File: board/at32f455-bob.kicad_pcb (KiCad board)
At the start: 2 copper layers, 66 parts, among them J1 BB, J2 PWR, J3 PROG, J4 CAN, J5 RS486, J6 USB_C_Receptacle, J7 +3.3V, J8 +5V, SW1 RotaryEncoder_Switch, SW2 RESET, SW3 BTL, U1 LM1117MP-3.3, U2 AT32F455CxT7, U3 PAN2110P0AA, U4 HMT1040T, U5 ST3485EB, U6 ER_OLEDM0.91_1x-I2C, Y1 not populated, Y2 16MHz

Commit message: WIP
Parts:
- J4, J5: footprint Connector_Phoenix_MC:PhoenixContact_MCV_1,5_3-G-3.5_1x03_P3.50mm_Vertical -> Connector_Phoenix_MC:PhoenixContact_MC_1,5_3-G-3.5_1x03_P3.50mm_Horizontal
- J7, J8: footprint Connector_Phoenix_MC:PhoenixContact_MCV_1,5_2-G-3.5_1x02_P3.50mm_Vertical -> Connector_Phoenix_MC:PhoenixContact_MC_1,5_2-G-3.5_1x02_P3.50mm_Horizontal
- moved D4 146.9 mm to (209.4, 52.0)
- moved D5 146.9 mm to (209.4, 55.1)
- moved SW1 146.9 mm to (204.8, 28.4)
- moved C16 146.9 mm to (209.4, 40.0)
- moved C17 146.9 mm to (209.4, 43.0)
- moved C18 146.9 mm to (209.4, 46.0)
- moved C19 146.9 mm to (209.4, 49.0)
- moved D6 146.9 mm to (215.7, 41.8)
- moved R10 146.9 mm to (205.0, 51.8)
- moved R11 146.9 mm to (205.0, 54.7)
- moved R12 146.9 mm to (205.0, 57.6)
- moved R13 146.9 mm to (205.0, 60.6)
- moved R6 146.9 mm to (205.0, 40.0)
- moved R7 146.9 mm to (205.0, 42.9)
- moved R8 146.9 mm to (205.0, 45.9)
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
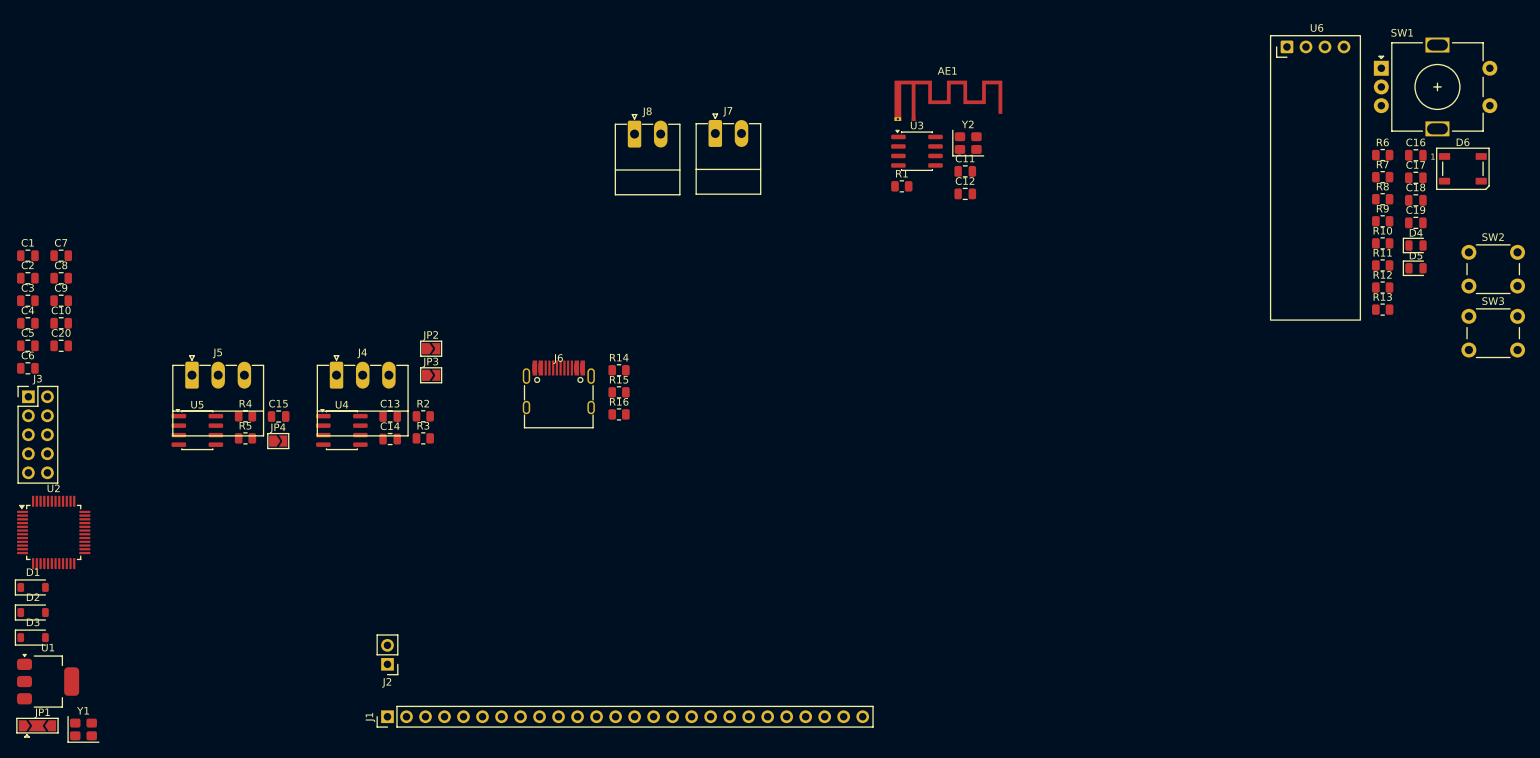
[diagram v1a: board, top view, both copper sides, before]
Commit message: Update board settings, schematic components, and add footprint library
- Changed active layer from 0 to 25 and updated hidden nets to include "GND" in at32f455-bob.kicad_prl.
- Modified selection filter settings to hide dimensions, graphics, keepouts, and other items in at32f455-bob.kicad_prl.
- Adjusted visible layers in at32f455-bob.kicad_prl for better clarity.
- Updated the position and orientation of the J5 connector in rs485.kicad_sch for improved layout.
- Added a new fp-lib-table file to define the footprint library for the project.
- Updated submodule reference for hw-kicad to the latest commit.
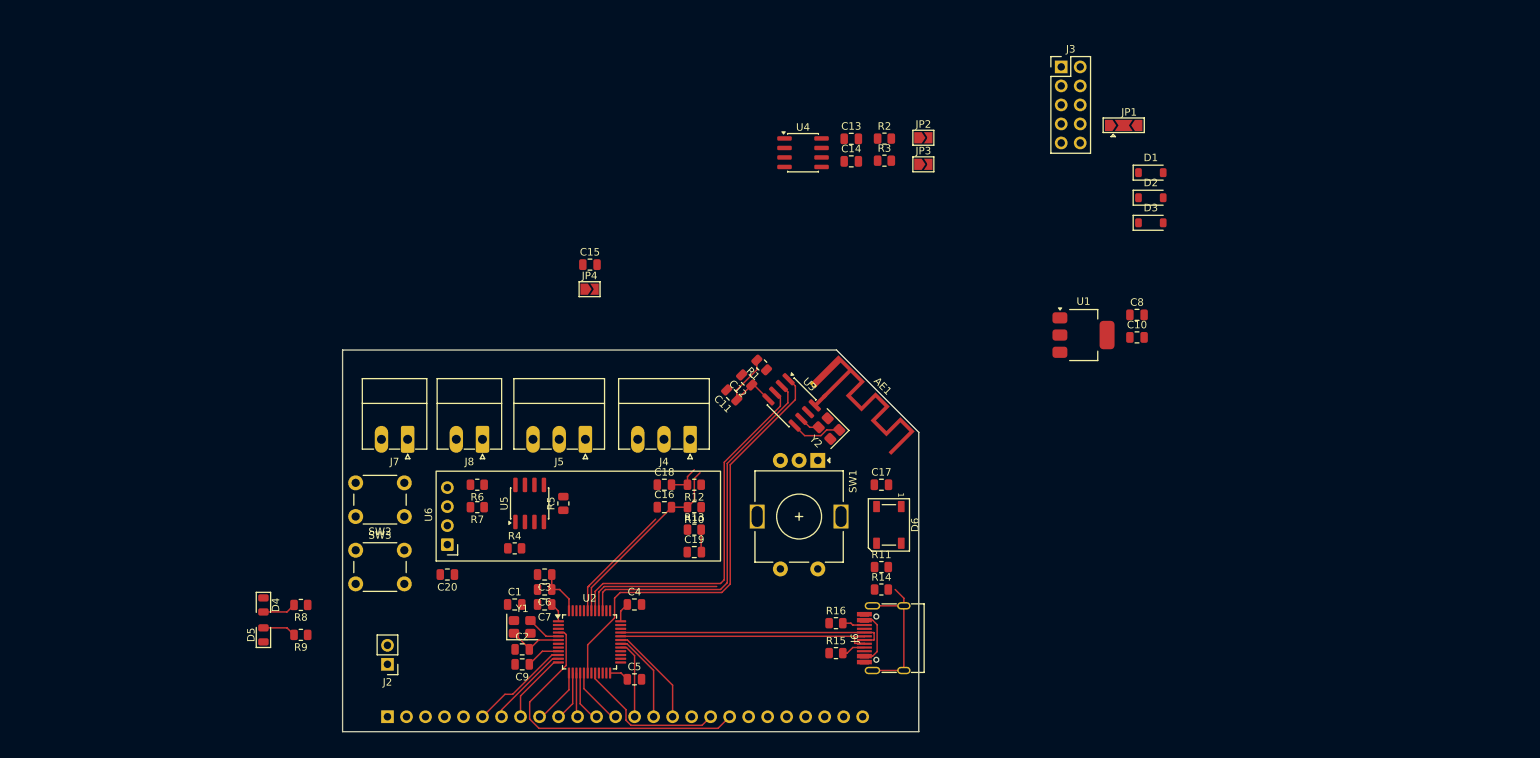
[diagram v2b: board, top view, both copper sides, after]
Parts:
- J1: moved to B.Cu
- moved JP1 165.8 mm to (170.4, 36.0)
- moved D5 161.6 mm to (55.4, 104.1), turned to 90 degrees
- moved D4 161.3 mm to (55.4, 100.1), turned to -90 degrees
- moved D1 159.3 mm to (174.0, 42.3)
- moved D2 159.3 mm to (174.0, 45.6)
- moved D3 159.3 mm to (174.0, 49.0)
- moved R9 154.8 mm to (60.4, 104.1), turned to 180 degrees
- moved R8 154.4 mm to (60.4, 100.1), turned to 180 degrees
- moved SW3 152.0 mm to (67.8, 92.8)
- moved SW2 146.6 mm to (74.2, 88.2), turned to 180 degrees
- moved U1 145.9 mm to (165.0, 64.0)
- moved J3 144.9 mm to (162.0, 28.2)
- moved C8 143.8 mm to (172.2, 61.3)
- moved C10 143.8 mm to (172.2, 64.3)
- moved U6 130.4 mm to (80.0, 92.0), turned to 90 degrees
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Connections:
- JP4 pad 2: Net-(J5-Pin_3) -> Net-(J5-Pin_1)
- R5 pad 1: Net-(J5-Pin_1) -> Net-(J5-Pin_3)
- U5 pad 6: Net-(J5-Pin_3) -> Net-(J5-Pin_1)
- U5 pad 7: Net-(J5-Pin_1) -> Net-(J5-Pin_3)
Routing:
- net /~{BLERIOT_CS}: track 0.00 -> 59.1 mm
- net /BLERIOT_SCK: track 0.00 -> 49.6 mm
- net /BLERIOT_DATA: track 0.00 -> 48.9 mm
- net /PC15: track 0.00 -> 42.3 mm
- net /USB_D+: track 0.00 -> 36.1 mm
- net /USB_D-: track 0.00 -> 34.9 mm
- net +3.3V: track 0.00 -> 31.2 mm
- net /ENC_A: track 0.00 -> 25.7 mm
- net /ENC_SW: track 0.00 -> 21.6 mm
- net /ENC_B: track 0.00 -> 20.7 mm
- net /PB2: track 0.00 -> 20.1 mm
- net Net-(J6-SHIELD): track 0.00 -> 19.7 mm
- net /PA10: track 0.00 -> 13.7 mm
- net /PA0: track 0.00 -> 13.6 mm
- net /PA9: track 0.00 -> 12.1 mm
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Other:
- board outline added: 77 x 51 mm
